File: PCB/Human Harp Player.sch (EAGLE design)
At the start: 39 parts, among them J1 4UCON 20404, J3 Sparkfun: PRT-00553, J4 Sparkfun: PRT-00553, J5 Sparkfun: PRT-00553, J6 Sparkfun: PRT-00553, J7 ICSP, J8 Molex: 500075-1517, Q1 MMBT2222A, Q3 STD26P3LLH6, U1 DSPIC33EP512GM604-I/PT, U2 MIC5319-3.3YD5, U3 Sparkfun: PRT-00116, X1 ABM8-16.000MHZ-B2-T

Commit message: Commit PCB Rev. 2
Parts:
- removed J6: Sparkfun: PRT-00553, SparkFun:M06SIP
- removed J7: ICSP, SparkFun-Connectors:M06NO_SILK
- removed J8: Molex: 500075-1517, x-io:USB-5PIN
- removed LED1: Sparkfun: COM-12903 (purple), SparkFun-LED:LED5MM
- removed Q3: STD26P3LLH6, transistor-fet:SPD30P06PTO252
- removed R10: 10k, 0603, SparkFun:RESISTOR0402-RES
- removed R11: 15R, 0603, SparkFun:RESISTOR0402-RES
- removed S1: RS: 5MS1S102AM2QES, x-io:SWITCH-DPST5MS1S102AM2QES
- removed S2: TE Connectivity: FSM4JAH, SparkFun-Electromechanical:SWITCH-MOMENTARY-2PTH
- removed U$4: OSHW_LOGO6MM_BOTTOM, x-io:OSHW_LOGO6MM_BOTTOM
- added C12, C15, C16: 100n, 0603, SparkFun:CAP0402-CAP
- added C13, C14: 22p, 0603, SparkFun:CAP0402-CAP
- added J2: Unpopulated, SparkFun-Connectors:M05PTH
- added L1: 220u, 510mA, EATON-DRA73-221-R, rcl:L-USPIS2816
- added LOGO1: OSHW-LOGOL, SparkFun-Aesthetics:OSHW-LOGOL
- added Q2: IRLML6401PBF, SparkFun-DiscreteSemi:MOSFET-PCHANNEL
- added U4: DSPIC33EP512GM604-I/PT, x-io:DSPIC33EP512GM604
- added U5, U6: WS2811, SparkFun-LED:LED-TRICOLOR-5050-ICWS2811
- C1: value 100n, 0603 -> 470u, 16V, Pansonic F; device SparkFun:CAP0402-CAP -> rcl:CPOL-USF
- C10, C8: value 100n, 0603 -> 10u, 0603
- C11: value 470u, 10V, Tant, Case E -> 10u, 0603; device rcl:CPOL-USSMCE -> SparkFun:CAP0402-CAP
- C5, C6: value 22p, 0603 -> 100n, 0603
- C9: value 10u, 0603 -> 100n, 0603
- J1: value 4UCON 20404 -> Sparkfun-PRT-00587; device x-io:JST -> SparkFun-Connectors:USBSMD
- J3: value Sparkfun: PRT-00553 -> Sparkfun: PRT-00116
- J4: value Sparkfun: PRT-00553 -> Unpopulated; device SparkFun-Connectors:M05PTH -> SparkFun-Connectors:M06NO_SILK
- J5: value Sparkfun: PRT-00553 -> Sparkfun: PRT-00116; device SparkFun-Connectors:M03PTH -> SparkFun-Connectors:M05PTH
- Q1: value MMBT2222A -> IRLML6401PBF; device SparkFun-DiscreteSemi:TRANSISTOR_NPNMMBT2222A -> SparkFun-DiscreteSemi:MOSFET-PCHANNEL
- R1, R6, R7: value 10k 0603 -> 4k7, 0603
- R2, R3, R4, R5, R8, R9: value 10k, 0603 -> 4k7, 0603
- U1: value DSPIC33EP512GM604-I/PT -> FT232RL; device x-io:DSPIC33EP512GM604 -> SparkFun:FT232RLSSOP
- U2: value MIC5319-3.3YD5 -> BMX055; device x-io:MIC5319 -> x-io:BMX055
- U3: value Sparkfun: PRT-00116 -> MIC5319-3.3YD5; device x-io-EAGLE-Library:X-OSC-TH -> x-io:MIC5319
- X1: value ABM8-16.000MHZ-B2-T -> ABRACON-ABM8-16.000MHZ-B2-T
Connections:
- removed net AUX: J7.6, U1.OA3OUT/AN6/C3IN4-/C4IN4-/C4IN1+/RP48/OCFB/RC0
- removed net BATTERY_LEVEL: C10.1, R6.1, R7.2, U1.OA2OUT/AN0/C2IN4-/C5IN2-/C4IN3-/RPI16/RA0
- removed net BUTTON: S2.2, U1.OA3IN-/AN7/C3IN1-/C4IN1-/RP49/RC1
- removed net ENCODER_VDD: J3.2, R2.2, R3.2, U1.AN28/SDI1/RPI25/RA9
- removed net IMU_INT: J4.4, U1.AN29/SCK1/RPI51/RC3
- removed net IMU_SCL: J4.3, R4.1, U1.AN31/CVREF2O/SCL1/RPI53/RC5
- removed net IMU_SDA: J4.1, R5.1, U1.AN30/SDA1/RPI52/RC4
- removed net IMU_VDD: J4.2, R4.2, R5.2, U1.PGED2/ASDA2/RP37/RB5
- removed net IN1: J6.2, U1.TCK/AN26/TDO/PWM4H/RA10/CVREF1O/ASCL1/RP40/T4CK/RB8, U3.IN1
- removed net LED: R11.1, U1.OA5IN+/AN24/C5IN3-/C5IN1+/SDO1/RP20/T1CK/RA4
- removed net OUT1: J6.3, U1.OA5OUT/AN25/C5IN4-/RP39/INT0/RB7, U3.OUT1
- removed net OUT16: J5.3, U3.OUT16
- removed net POWER_ENABLE: U1.TMS/OA5IN-/AN27/C5IN1-/ASDA1/SDI1/RP41/RB9
- removed net VIN: C11.+, C7.1, Q3.S, R6.2, R9.2, S1.2, U2.EN, U2.VIN
- removed net X-OSC_ENABLE: R10.2, R8.1
- removed net X-OSC_PWR: J5.2, Q3.D, U3.BATTERY
- new net 3V3: C10.1, C12.1, C15.1, C16.2, R5.1, U3.VOUT, U4.AVDD, U4.VDD, U4.VDD@1
- new net 5V: C8.1, J3.2, Q1.D, R3.2, R4.2, U3.EN, U3.VIN, U5.VDD, U6.VDD
- new net BMX055_INT: J2.4, J5.4, U2.INT3, U4.AN29/SCK1/RPI51/RC3
- new net BMX055_SCL: J2.3, J5.3, R8.1, U2.SCX, U4.AN31/CVREF2O/SCL1/RPI53/RC5
- new net BMX055_SDA: J2.1, J5.1, R9.1, U2.SDX, U4.AN30/SDA1/RPI52/RC4
- new net FTDI_D+: J1.D+, U1.USBDP
- new net FTDI_D-: J1.D-, U1.USBDM
- new net FTDI_RX: R6.1, U1.RXD
- new net FTDI_SLEEP: Q2.G, R1.2, U1.SLEEP
- new net FTDI_TX: R7.1, U1.TXD
- new net N$6: J1.VBUS, L1.1
- new net N$8: U5.DO, U6.DI
- new net TEST: J4.6, U4.OA3OUT/AN6/C3IN4-/C4IN4-/C4IN1+/RP48/OCFB/RC0
- new net VSENSORS: C5.1, C6.1, C7.2, J2.2, J5.2, R8.2, R9.2, U2.PS, U2.VDD, U2.VDDIO, U4.PGED2/ASDA2/RP37/RB5
- new net WS2811_DATA: U4.RP54/PWM6H/RC6, U5.DI
- net ENCODER_A: now also R3.1, U4.SDA2/RPI24/RA8; no longer R2.1, U1.SDA2/RPI24/RA8
- net ENCODER_B: now also R4.1, U4.FLT32/SCL2/RP36/RB4; no longer R3.1, U1.FLT32/SCL2/RP36/RB4
- net GND: now also C1.-, C11.2, C12.2, C13.1, C14.1, C15.2, C16.1, C2.1, C3.1, C7.1, J1.GND, J2.5, J4.3, J5.5, R1.1, R2.1, U1.AGND, U1.CTS, U1.GND18, U1.GND21, U1.GND7, U1.TEST, U2.CSB3, U2.GNDA, U2.GNDIO, U2.SDO1, U2.SDO2, U3.GND, U4.AVSS, U4.VSS, U4.VSS@1, U4.VSS@2, U5.VSS, U6.VSS, X1.@2, X1.@4; no longer C1.2, C11.-, C2.2, C3.2, C7.2, J1.@-, J4.5, J5.1, J6.5, J6.6, J7.3, J8.GND, LED1.C, Q1.E, R7.1, S2.1, U1.AVSS, U1.VSS, U1.VSS@1, U1.VSS@2, U2.GND, U3.GROUND@1, X1.GND, X1.GND@1
- net MCLR: now also J4.1, R5.2, U4.MCLR; no longer J7.1, R1.2, U1.MCLR
- net N$1: now also Q1.G, Q2.D, R2.2; no longer Q1.B, R10.1
- net N$2: now also R6.2, U4.TCK/AN26/TDO/PWM4H/RA10/CVREF1O/ASCL1/RP40/T4CK/RB8; no longer J1.@+, S1.3
- net N$3: now also C4.2, U1.3V3OUT; no longer LED1.A, R11.2
- net N$4: now also C11.1, U4.VCAP; no longer C2.1, U1.VCAP
- net N$5: now also R7.2, U4.OA5OUT/AN25/C5IN4-/RP39/INT0/RB7; no longer Q1.C, Q3.G, R9.1
- net N$7: now also C9.1, U3.BYP; no longer C8.1, U2.BYP
- net OSC1: now also C13.2, U4.AN32/OSC1/CLKI/RPI18/RA2, X1.@3; no longer C6.1, U1.AN32/OSC1/CLKI/RPI18/RA2, X1.XTAL
- net OSC2: now also C14.2, U4.OSC2/CLKO/RPI19/RA3, X1.@1; no longer C5.1, U1.OSC2/CLKO/RPI19/RA3, X1.XTAL@1
- net PGEC1: now also J4.5, U4.PGEC1/OA1IN+/AN4/C1IN3-/C1IN1+/C2IN3-/RPI34/RB2; no longer J7.5, U1.PGEC1/OA1IN+/AN4/C1IN3-/C1IN1+/C2IN3-/RPI34/RB2
- net PGED1: now also J4.4, U4.PGED1/OA1IN-/AN5/C1IN1-/CTMUC/RP35/RB3; no longer J7.4, U1.PGED1/OA1IN-/AN5/C1IN1-/CTMUC/RP35/RB3
- net VBUS: now also C1.+, C2.2, C3.2, L1.2, Q1.S, Q2.S, U1.VCC, U1.VCCIO; no longer J6.4, J8.VBUS, S1.1
- net VDD: now also J4.2; no longer C1.1, C3.1, C4.2, C9.1, J7.2, R1.1, R8.2, U1.AVDD, U1.VDD, U1.VDD@1, U2.VOUT
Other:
- note added: "5V enabled when FTDI_SLEEP is low FTDI CTS input pulled low to ensure FTDI transmission when hardware flow control enabled"
- note added: "Avago Technologies HEDS-5600-A06"
- note added: "BMX055 circuit based on page 159 of datasheet BMX055 gyroscope I2C slave address = 0x68 (because SDO2 is pulled low) BMX055 accelerometer I2C slave address = 0x18 (because CBS3 is pulled low) BMX055 magnetometer I2C slave address = 0x10 (because SDO1 is pulled low)"
- note added: "Encoder header"
- note added: "IMU daughterboard"
- note added: "IMU header"
- note added: "RB8 and RB7 are not 5V tollerant but can clamp up to 5 mA (see page 1 of DSPIC33EP512GM604 datasheet) RA8 (ENCODER_A) and RB4 (ENCODER_B) are 5V tolerant pins"
- note added: "RGB LEDs"
- note added: "Rev. 2"
- note added: "USB interface"
- note removed: "Avago Technologies HEDS-5600"
- note removed: "Battery level"
- note removed: "Battery/USB power supply"
- note removed: "Bosch BMX055"
- note removed: "Button"
- note removed: "Encoder"
- note removed: "FTDI"
- note removed: "From datasheet: "Exceptions are: RA3, RA4, RA7, RA9, RA10, RB7-RB15, RC3, RC15, RD1-RD4, which are able to sink 30 mA and source 20 mA.""
- note removed: "IMU"
- note removed: "LED"
- note removed: "NeoPixels"
- note removed: "Requires dsPIC33EP internal pull-up"
- note removed: "Sparkfun DEV-09716 (FTDI Basic Breakout - 5V)"
- note removed: "Typical quiescent current = 90uA"
- note removed: "x-OSC"
- note removed: "x-OSC power enable"
- moved on the sheet: C10, C2, C3, C4, C5, C6, C7, C8, C9, J3, R1, R2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

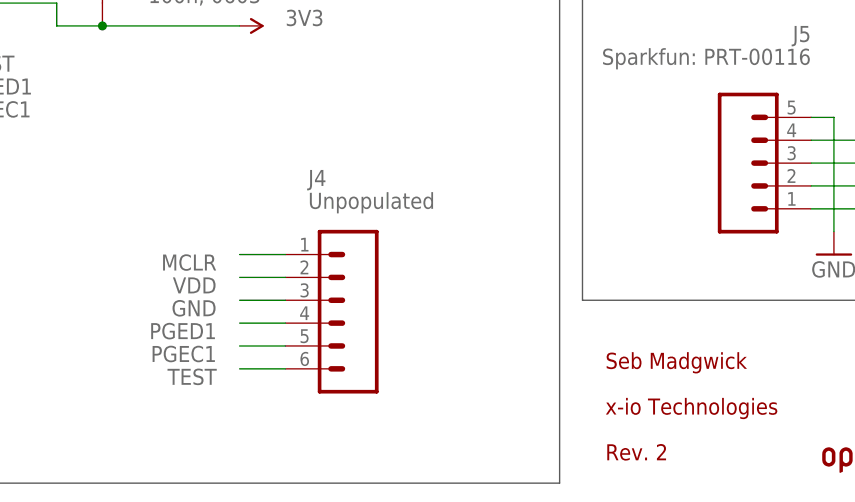
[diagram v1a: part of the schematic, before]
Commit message: Add missing VDD connection to ICSP and XYZ label on PCB
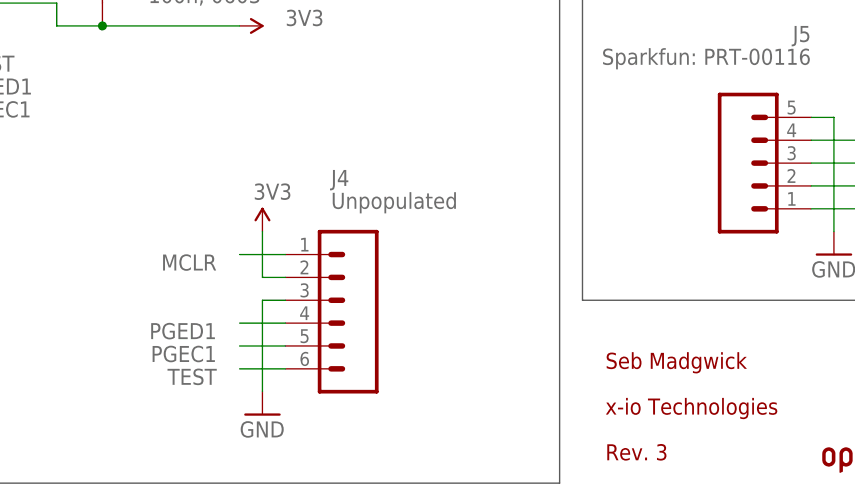
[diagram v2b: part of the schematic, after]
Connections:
- removed net VDD: J4.2
- net 3V3: now also J4.2
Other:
- note added: "Rev. 3"
- note removed: "Rev. 2"
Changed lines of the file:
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@@
 <part name="GND28" library="SparkFun-Aesthetics" deviceset="GND" device=""/>
 <part name="SUPPLY21" library="x-io" deviceset="VSENSORS" device=""/>
+<part name="GND29" library="SparkFun-Aesthetics" deviceset="GND" device=""/>
+<part name="SUPPLY22" library="x-io" deviceset="3V3" device=""/>
 </parts>
 <sheets>
@@
 <text x="7.62" y="7.62" size="1.778" layer="97">RB8 and RB7 are not 5V tollerant but can clamp up to 5 mA (see page 1 of DSPIC33EP512GM604 datasheet)
 RA8 (ENCODER_A) and RB4 (ENCODER_B) are 5V tolerant pins</text>
-<text x="292.1" y="7.62" size="1.778" layer="94" font="vector">Rev. 2</text>
+<text x="292.1" y="7.62" size="1.778" layer="94" font="vector">Rev. 3</text>
 </plain>
 <instances>
@@
 </instance>
 <instance part="J4" gate="G$1" x="261.62" y="25.4" smashed="yes" rot="R180">
-<attribute name="VALUE" x="259.08" y="35.56" size="1.778" layer="96"/>
-<attribute name="NAME" x="259.08" y="38.1" size="1.778" layer="95"/>
+<attribute name="VALUE" x="261.62" y="35.56" size="1.778" layer="96"/>
+<attribute name="NAME" x="261.62" y="38.1" size="1.778" layer="95"/>
 </instance>
 <instance part="X1" gate="G$1" x="182.88" y="25.4" smashed="yes" rot="R90">
@@
 <attribute name="VALUE" x="223.52" y="93.98" size="1.778" layer="96"/>
 </instance>
+<instance part="GND29" gate="1" x="254" y="12.7"/>
+<instance part="SUPPLY22" gate="3V3" x="254" y="33.02"/>
 </instances>
 <busses>
@@
 </segment>
 <segment>
-<wire x1="256.54" y1="25.4" x2="251.46" y2="25.4" width="0.1524" layer="91"/>
-<label x="248.92" y="25.4" size="1.778" layer="95" rot="R180"/>
+<wire x1="256.54" y1="25.4" x2="254" y2="25.4" width="0.1524" layer="91"/>
 <pinref part="J4" gate="G$1" pin="3"/>
+<pinref part="GND29" gate="1" pin="GND"/>
+<wire x1="254" y1="15.24" x2="254" y2="25.4" width="0.1524" layer="91"/>
 </segment>
 <segment>
@@
 </segment>
 </net>
-<net name="VDD" class="0">
-<segment>
-<wire x1="256.54" y1="27.94" x2="251.46" y2="27.94" width="0.1524" layer="91"/>
-<label x="248.92" y="27.94" size="1.778" layer="95" rot="R180"/>
-<pinref part="J4" gate="G$1" pin="2"/>
-</segment>
-</net>
 <net name="MCLR" class="0">
 <segment>
@@
 <pinref part="SUPPLY16" gate="3V3" pin="3V3"/>
 </segment>
-</net>
+<segment>
+<wire x1="256.54" y1="27.94" x2="254" y2="27.94" width="0.1524" layer="91"/>
+<pinref part="J4" gate="G$1" pin="2"/>
+<pinref part="SUPPLY22" gate="3V3" pin="3V3"/>
+<wire x1="254" y1="33.02" x2="254" y2="27.94" width="0.1524" layer="91"/>
+</segment>
+</net>
